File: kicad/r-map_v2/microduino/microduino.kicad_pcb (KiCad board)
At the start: 2 copper layers, 25.4 x 29.2 mm, 16 parts, among them P1 CONN_01X02, P2 CONN_RELE_BOARD, P3 CONN_01X05, P4 CONFIG, P5 USB_OTG, P6 CONN_01X01, P7 CONN_01X01, U1 Microduino, U2 ESDA6V1-5SC6, U3 REG113NA-3.3/250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

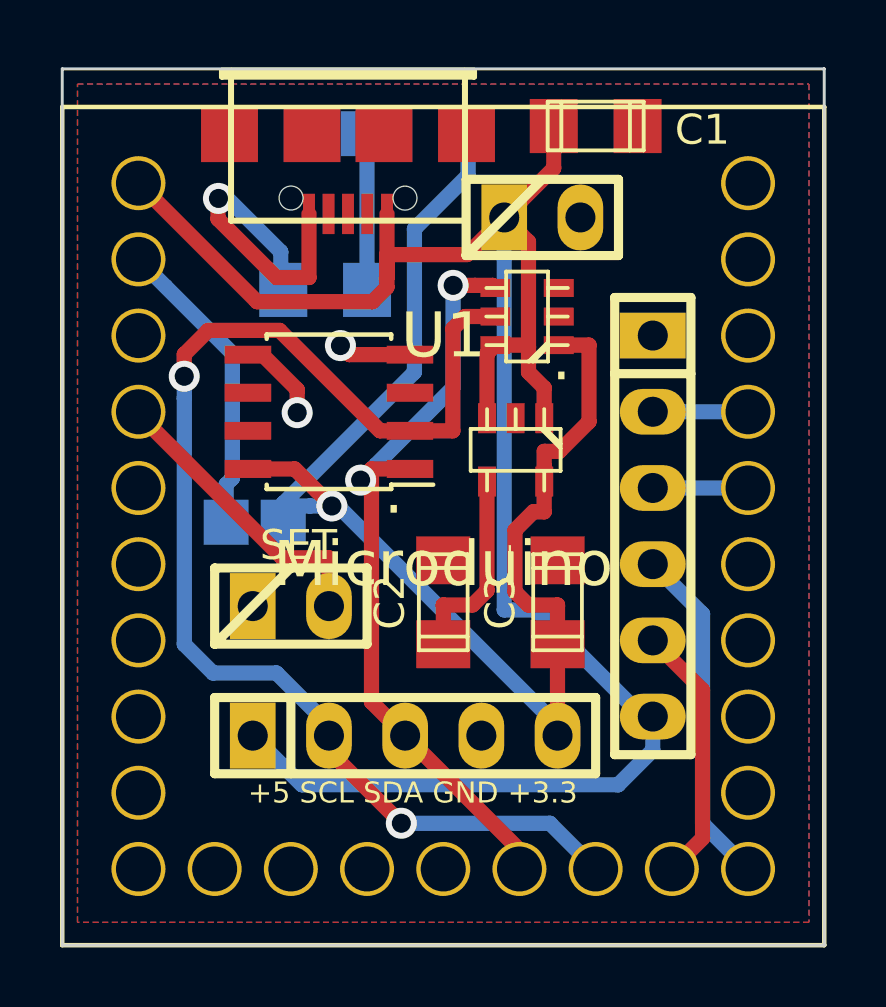
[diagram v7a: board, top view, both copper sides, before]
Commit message: Aggiunti gerber files per breakout board e sistemato case led stima-i2c
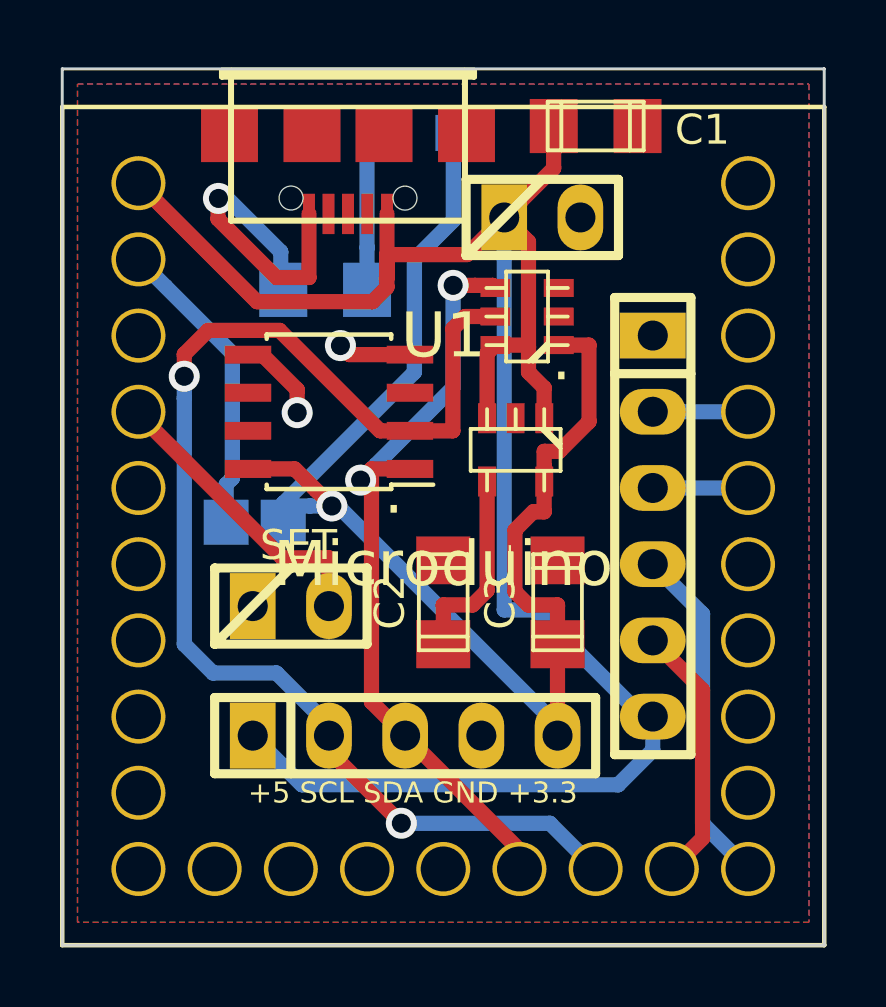
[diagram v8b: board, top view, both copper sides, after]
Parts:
- D1: footprint w_smd_leds:Led_1206 -> w_smd_leds:Led_0805
- moved D1 0.21 mm to (147.9, 91.0)
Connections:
- D1 pad 1: Net-(D1-Pad1) -> /+3.3V
- D1 pad 2: /+3.3V -> Net-(D1-Pad1)
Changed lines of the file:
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@@
-(kicad_pcb (version 4) (host pcbnew 0.201512051503+6347~38~ubuntu14.04.1-stable)
+(kicad_pcb (version 4) (host pcbnew 0.201601131446+6458~42~ubuntu14.04.1-product)
   (general
     (links 43)
     (no_connects 0)
-    (area 135.560999 88.21928 161.619001 118.439001)
+    (area 135.560999 88.19388 161.619001 118.439001)
     (thickness 1.6)
     (drawings 16)
-    (tracks 137)
+    (tracks 139)
     (zones 0)
     (modules 16)
@@
     (35 F.Paste user hide)
     (36 B.SilkS user)
-    (37 F.SilkS user)
+    (37 F.SilkS user hide)
     (38 B.Mask user)
     (39 F.Mask user)
@@
     (mod_text_size 1 1)
     (mod_text_width 0.2)
-    (pad_size 1.50114 1.50114)
+    (pad_size 1.19888 1.19888)
     (pad_drill 0)
     (pad_to_mask_clearance 0.2)
@@
     (visible_elements 7FFFFF7F)
     (pcbplotparams
-      (layerselection 0x010f0_80000001)
+      (layerselection 0x010f0_ffffffff)
       (usegerberextensions false)
       (excludeedgelayer true)
@@
     (add_net "Net-(P6-Pad1)")
   )
+  (module w_smd_leds:Led_0805 (layer B.Cu)
+    (at 147.8788 91.0336)
+    (descr "SMD LED, 0805")
+    (fp_text reference D1 (at 0 1.651) (layer B.SilkS)
+      (effects (font (size 0.8001 0.8001) (thickness 0.14986)) (justify mirror))
+    )
+    (fp_text value LED_SMD (at 0 -1.80086) (layer B.SilkS)
+      (effects (font (size 0.8001 0.8001) (thickness 0.14986)) (justify mirror))
+    )
+    (fp_line (start -0.13716 0) (end 0.16256 0.29972) (layer B.SilkS) (width 0.127))
+    (fp_line (start 0.16256 0.29972) (end 0.16256 -0.29972) (layer B.SilkS) (width 0.127))
+    (fp_line (start 0.16256 -0.29972) (end -0.13716 0) (layer B.SilkS) (width 0.127))
+    (fp_line (start -0.03556 -0.09906) (end -0.03556 0.09906) (layer B.SilkS) (width 0.127))
+    (fp_line (start 0.0635 0.20066) (end 0.0635 -0.20066) (layer B.SilkS) (width 0.127))
+    (fp_line (start 0.29972 -0.8001) (end 0.29972 0.8001) (layer B.SilkS) (width 0.127))
+    (fp_line (start -0.29972 0.8001) (end -0.29972 -0.8001) (layer B.SilkS) (width 0.127))
+    (fp_line (start -1.00076 0.8001) (end 1.00076 0.8001) (layer B.SilkS) (width 0.127))
+    (fp_line (start 1.00076 0.8001) (end 1.00076 -0.8001) (layer B.SilkS) (width 0.127))
+    (fp_line (start 1.00076 -0.8001) (end -1.00076 -0.8001) (layer B.SilkS) (width 0.127))
+    (fp_line (start -1.00076 -0.8001) (end -1.00076 0.8001) (layer B.SilkS) (width 0.127))
+    (pad 2 smd rect (at -1.04902 0) (size 1.19888 1.19888) (layers B.Cu B.Paste B.Mask)
+      (net 13 "Net-(D1-Pad1)"))
+    (pad 1 smd rect (at 1.04902 0) (size 1.19888 1.19888) (layers B.Cu B.Paste B.Mask)
+      (net 9 /+3.3V))
+    (model walter/smd_leds/led_0805.wrl
+      (at (xyz 0 0 0))
+      (scale (xyz 1 1 1))
+      (rotate (xyz 0 0 0))
+    )
+  )
   (module w_smd_resistors:r_1206 (layer B.Cu)
     (at 144.653 96.266)
@@
     (pad 1 smd rect (at 0 0) (size 1.50114 1.50114) (layers B.Cu B.Paste B.Mask)
       (net 12 "Net-(P6-Pad1)"))
-  )
-  (module w_smd_leds:Led_1206 (layer B.Cu)
-    (at 147.67052 91.059)
-    (descr "SMD LED_ 1206")
-    (fp_text reference D1 (at -3.81 0) (layer B.SilkS)
-      (effects (font (size 1 1) (thickness 0.175)) (justify mirror))
-    )
-    (fp_text value LED_SMD (at 0 -1.80086) (layer B.SilkS) hide
-      (effects (font (size 0.8001 0.8001) (thickness 0.14986)) (justify mirror))
-    )
-    (fp_line (start 0 0.20066) (end 0 -0.09906) (layer B.SilkS) (width 0.254))
-    (fp_line (start -0.09906 -0.29972) (end -0.09906 0.29972) (layer B.SilkS) (width 0.254))
-    (fp_line (start -0.29972 0.59944) (end -0.29972 -0.59944) (layer B.SilkS) (width 0.254))
-    (fp_line (start -0.29972 -0.59944) (end 0.29972 0) (layer B.SilkS) (width 0.254))
-    (fp_line (start 0.29972 0) (end -0.29972 0.59944) (layer B.SilkS) (width 0.254))
-    (fp_line (start 0.8001 -0.89916) (end 0.8001 0.89916) (layer B.SilkS) (width 0.254))
-    (fp_line (start -0.8001 0.89916) (end -0.8001 -0.89916) (layer B.SilkS) (width 0.254))
-    (fp_line (start -1.6002 0.89916) (end 1.6002 0.89916) (layer B.SilkS) (width 0.254))
-    (fp_line (start 1.6002 0.89916) (end 1.6002 -0.89916) (layer B.SilkS) (width 0.254))
-    (fp_line (start 1.6002 -0.89916) (end -1.6002 -0.89916) (layer B.SilkS) (width 0.254))
-    (fp_line (start -1.6002 -0.89916) (end -1.6002 0.89916) (layer B.SilkS) (width 0.254))
-    (pad 1 smd rect (at -1.74752 0) (size 1.4986 1.4986) (layers B.Cu B.Paste B.Mask)
-      (net 13 "Net-(D1-Pad1)"))
-    (pad 2 smd rect (at 1.74752 0) (size 1.4986 1.4986) (layers B.Cu B.Paste B.Mask)
-      (net 9 /+3.3V))
-    (model walter/smd_leds/led_1206.wrl
-      (at (xyz 0 0 0))
-      (scale (xyz 1 1 1))
-      (rotate (xyz 0 0 0))
-    )
   )
   (module Rmap:microduino (layer F.Cu)
@@
   (segment (start 146.715 93.7336) (end 146.715 95.0737) (width 0.508) (layer F.Cu) (net 8))
   (segment (start 146.715 95.0737) (end 146.715 95.8277) (width 0.508) (layer F.Cu) (net 8))
-  (segment (start 149.41804 91.059) (end 149.41804 92.446757) (width 0.508) (layer B.Cu) (net 9))
+  (segment (start 143.256 103.3835) (end 147.629264 99.010236) (width 0.508) (layer B.Cu) (net 9))
+  (segment (start 147.629264 99.010236) (end 147.629264 95.247949) (width 0.508) (layer B.Cu) (net 9))
+  (segment (start 147.629264 95.247949) (end 148.92782 93.949393) (width 0.508) (layer B.Cu) (net 9))
+  (segment (start 148.92782 93.949393) (end 148.92782 91.0336) (width 0.508) (layer B.Cu) (net 9))
   (segment (start 142.08 102.235) (end 143.641992 102.235) (width 0.508) (layer F.Cu) (net 9))
   (segment (start 143.256 103.3835) (end 143.343281 103.470781) (width 0.508) (layer B.Cu) (net 9))
   (segment (start 144.360274 102.953282) (end 144.877773 103.470781) (width 0.508) (layer F.Cu) (net 9))
-  (segment (start 147.629264 94.235533) (end 147.629264 99.010236) (width 0.508) (layer B.Cu) (net 9))
   (segment (start 144.145918 103.470781) (end 144.877773 103.470781) (width 0.508) (layer B.Cu) (net 9))
   (segment (start 152.4 111.125) (end 152.4 110.78718) (width 0.508) (layer B.Cu) (net 9))
-  (segment (start 149.41804 92.446757) (end 147.629264 94.235533) (width 0.508) (layer B.Cu) (net 9))
   (segment (start 145.083601 103.470781) (end 144.877773 103.470781) (width 0.508) (layer B.Cu) (net 9))
   (segment (start 152.4 110.78718) (end 145.083601 103.470781) (width 0.508) (layer B.Cu) (net 9))
   (segment (start 143.641992 102.235) (end 144.360274 102.953282) (width 0.508) (layer F.Cu) (net 9))
   (segment (start 143.343281 103.470781) (end 144.145918 103.470781) (width 0.508) (layer B.Cu) (net 9))
-  (segment (start 147.629264 99.010236) (end 143.256 103.3835) (width 0.508) (layer B.Cu) (net 9))
   (via (at 144.877773 103.470781) (size 1.035) (drill 0.635) (layers F.Cu B.Cu) (net 9))
   (segment (start 152.4406 98.1075) (end 153.4493 98.1075) (width 0.508) (layer F.Cu) (net 9))
@@
   (segment (start 139.329999 96.149999) (end 138.43 95.25) (width 0.508) (layer B.Cu) (net 12))
   (segment (start 141.560813 102.544617) (end 141.560813 98.380813) (width 0.508) (layer B.Cu) (net 12))
-  (segment (start 146.05 96.266) (end 146.05 91.186) (width 0.508) (layer B.Cu) (net 13))
-  (segment (start 146.05 91.186) (end 145.923 91.059) (width 0.508) (layer B.Cu) (net 13))
+  (segment (start 146.82978 91.0336) (end 146.814851 91.0336) (width 0.508) (layer B.Cu) (net 13))
+  (segment (start 146.05 91.798451) (end 146.05 94.8563) (width 0.508) (layer B.Cu) (net 13))
+  (segment (start 146.814851 91.0336) (end 146.05 91.798451) (width 0.508) (layer B.Cu) (net 13))
+  (segment (start 146.05 94.8563) (end 146.05 96.266) (width 0.508) (layer B.Cu) (net 13))
   (zone (net 7) (net_name GND) (layer F.Cu) (hatch edge 0.508)
     (connect_pads yes (clearance 0.064))
